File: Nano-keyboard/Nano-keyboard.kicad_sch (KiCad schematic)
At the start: 41 parts, among them U1 QBC847BL, U2 ESP32-WROOM-32, U3 QBC847BL, U4 QBC847BL

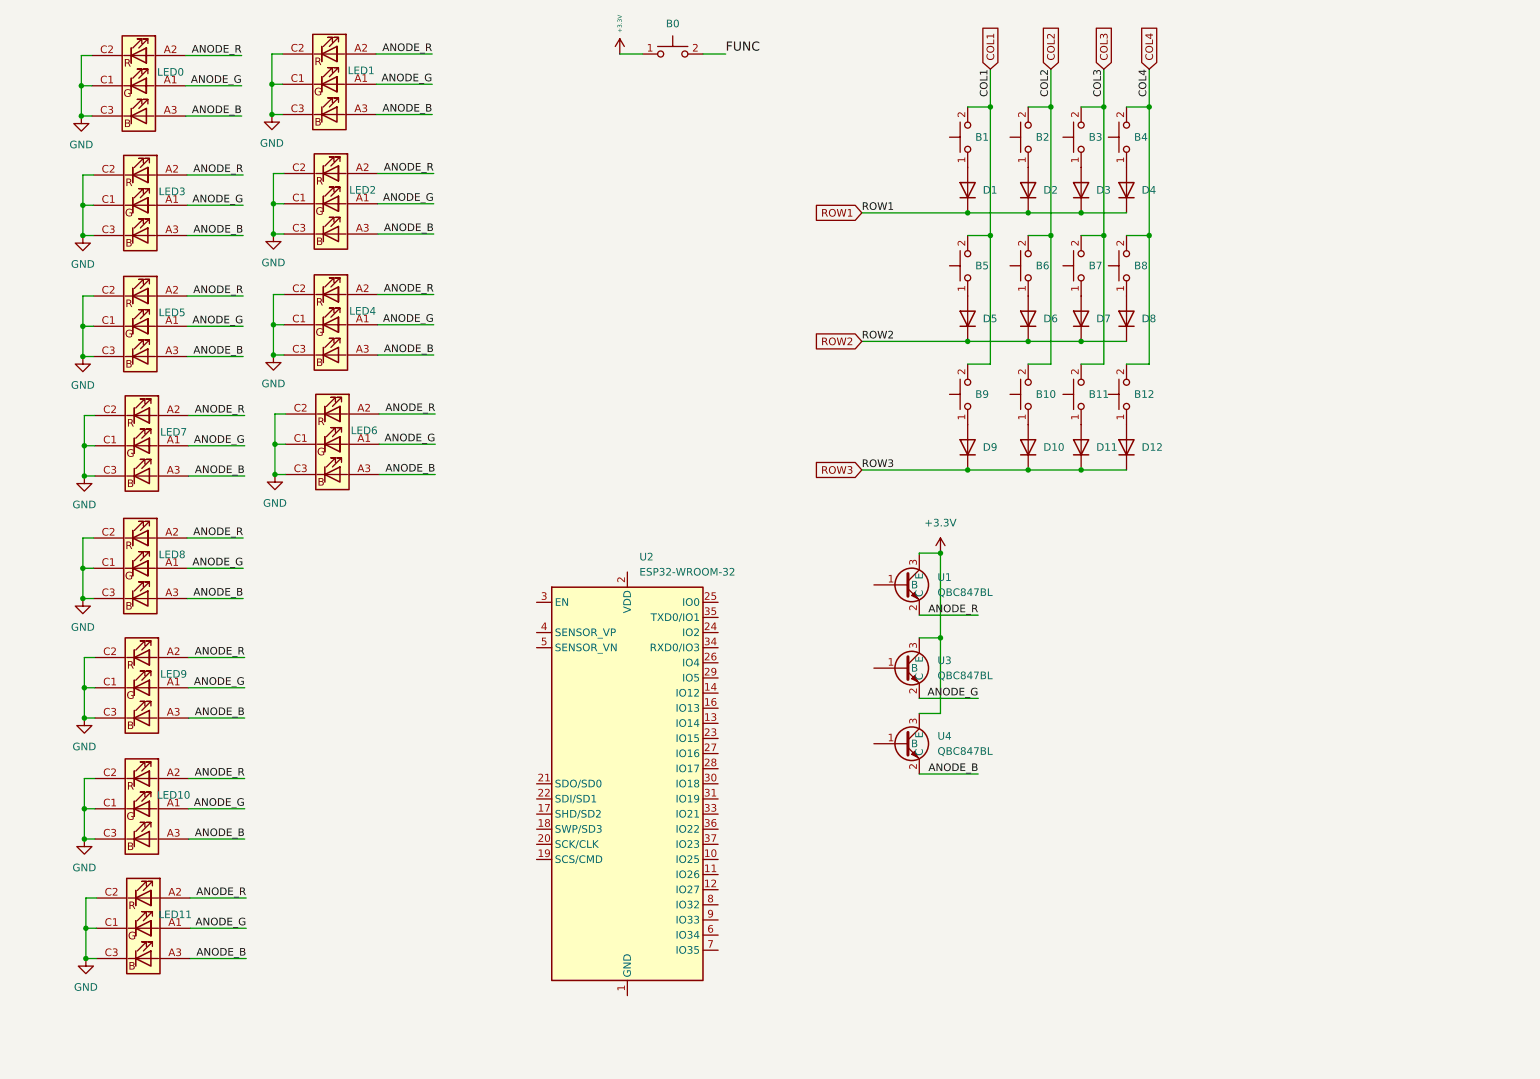
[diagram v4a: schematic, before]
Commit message: Charger Module and keyboard layout changes
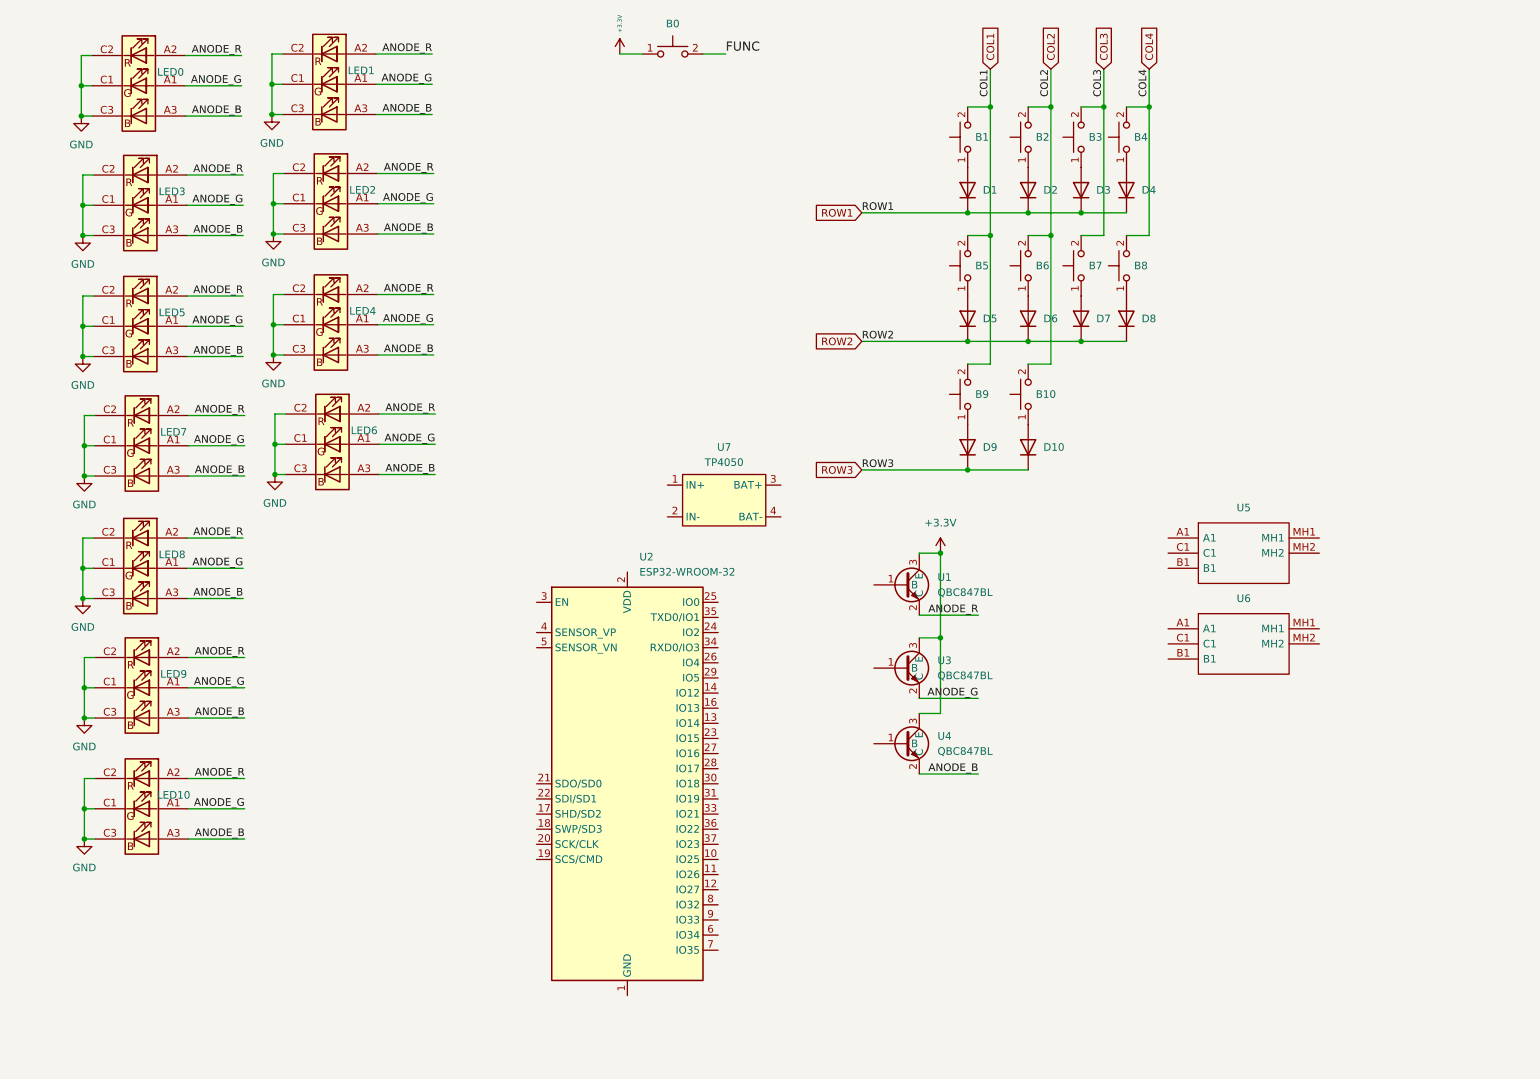
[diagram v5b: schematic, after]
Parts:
- removed B11, B12: Cherry_Switch_1U_PCB, lib:SW_Cherry_MX_1.00u_PCB, symbol custom-keyboard:Cherry_Switch_1U_PCB
- removed D11, D12: 1N914, Diode_THT:D_DO-35_SOD27_P3.81mm_Vertical_AnodeUp, symbol Diode:1N914
- removed LED11: LRTBGVSR-U4V2-JW+A6BB-D8+S2U2-7Z-20-S, lib:LRTBGVSRU4V2JWA6BBD8S2U27Z20S, symbol custom-keyboard:LRTBGVSR-U4V2-JW+A6BB-D8+S2U2-7Z-20-S
- added U5, U6: EN12-HN22AF25, lib:EN12HN22AF25, symbol custom-keyboard:EN12-HN22AF25
- added U7: TP4050, lib:TP4050-module, symbol custom-keyboard:TP4050
- D1, D10, D3, D4, D5, D6, D7, D8, D9: footprint Diode_THT:D_DO-35_SOD27_P3.81mm_Vertical_AnodeUp -> Diode_THT:D_DO-35_SOD27_P7.62mm_Horizontal

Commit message: Layout changes
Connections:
- net +3V3: now also U2.2 (VDD)
- net GND: now also U2.1 (GND), U2.15 (GND), U2.38 (GND), U2.39 (GND), U5.MH1, U5.MH2, U6.MH1, U6.MH2
- net LED_RED: now reaches U1.1 (B)
- net LED_RED: now also U2.9 (IO33)
- net BOOT: now reaches U2.25 (IO0)
- net LED_GREEN: now reaches U2.6 (IO34)
- net LED_GREEN: now also U3.1 (B)
- net LED_BLUE: now reaches U2.7 (IO35)
- net LED_BLUE: now also U4.1 (B)
- net at U5.C1: now also U6.C1
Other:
- moved on the sheet: U1, U2, U3, U4, U7

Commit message: Minor changes
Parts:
- removed LED1, LED10, LED2, LED3, LED4, LED5, LED6, LED7, LED8, LED9: LRTBGVSR-U4V2-JW+A6BB-D8+S2U2-7Z-20-S, lib:LRTBGVSRU4V2JWA6BBD8S2U27Z20S, symbol custom-keyboard:LRTBGVSR-U4V2-JW+A6BB-D8+S2U2-7Z-20-S
- removed U1, U3, U4: QBC847BL, lib:SOT96P237X111-3N, symbol custom-keyboard:QBC847BL
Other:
- moved on the sheet: U2, U5, U6

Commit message: Initial routing
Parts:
- removed U7: TP4050, lib:TP4050-module, symbol custom-keyboard:TP4050
- added U1: AMS1117, Package_TO_SOT_SMD:SOT-223-3_TabPin2, symbol Regulator_Linear:AMS1117
- added U3: J5019, lib:J5019-module, symbol custom-keyboard:J5019
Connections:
- net ANODE_B is gone; now on net LED_BLUE: LED0.A3
- net ANODE_G is gone; now on net LED_GREEN: LED0.A1
- net ANODE_R is gone; now on net LED_RED: LED0.A2
- net +3V3: now also U1.2 (VO)
- net COL1: now also U2.31 (IO19)
- net COL2: now also U2.33 (IO21)
- net COL3: now also U2.36 (IO22)
- net COL4: now also U2.37 (IO23)
- net FUNC: now also U2.30 (IO18)
- net GND: now also U3.4 (VOUT-)
- net ROW1: now also U2.16 (IO13)
- net ROW2: now also U2.23 (IO15)
- net ROW3: now also U2.24 (IO2)
- new net: U1.3 (VI), U3.3 (VOUT+)
